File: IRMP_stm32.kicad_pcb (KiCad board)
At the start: 2 copper layers, 10.5 x 22.5 mm, 29 parts, among them U1 TSOP773xx, U2 MIC5504-3.3YM5, U3 STM32F103T8Ux, X1 USB2_MICRO_B_F1

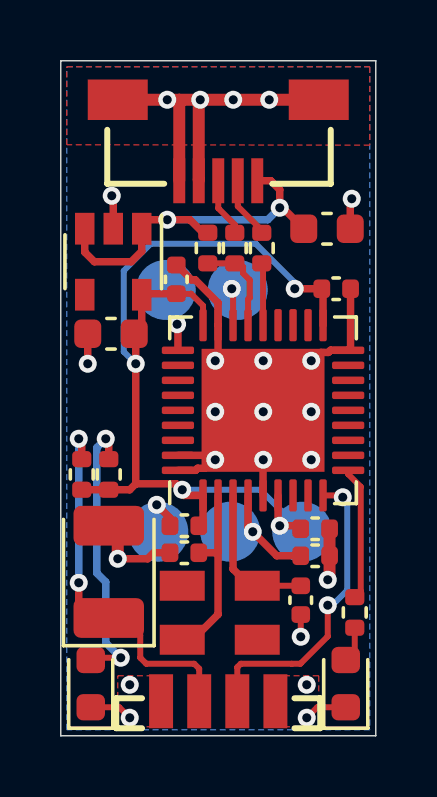
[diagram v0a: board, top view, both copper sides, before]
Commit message: Connect crystal lid to GND
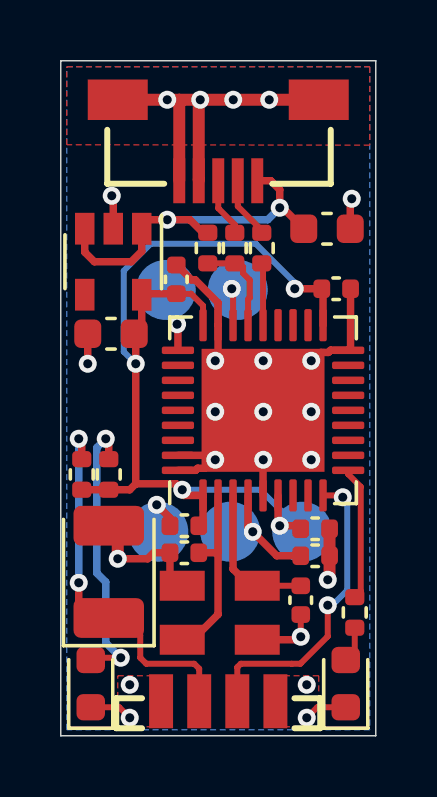
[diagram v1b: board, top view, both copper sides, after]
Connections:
- XC1 pad 2: Net-(XC1-Pad2) -> GNDD
- XC1 pad 4: Net-(XC1-Pad4) -> GNDD
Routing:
- net GNDD: track 44.9 -> 47.7 mm

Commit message: Set crystal frequency to 8MHz
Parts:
- XC1: value CRYSTAL_4pin -> 8MHz

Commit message: Update component values
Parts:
- U1: value TSOP773xx -> TSOP77338
- U3: value STM32F103T8Ux -> STM32F103T8U6
- X1: value USB2_MICRO_B_F1 -> 10118192-0001LF
